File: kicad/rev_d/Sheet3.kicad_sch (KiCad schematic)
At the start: 118 parts, among them X10 ST-214C, X14 AAFP/AC97 headphones/tapein, X16 PLB1-4I, X17 PLB1-4I, X18 PLB1-4I, X20 PLB1-4I

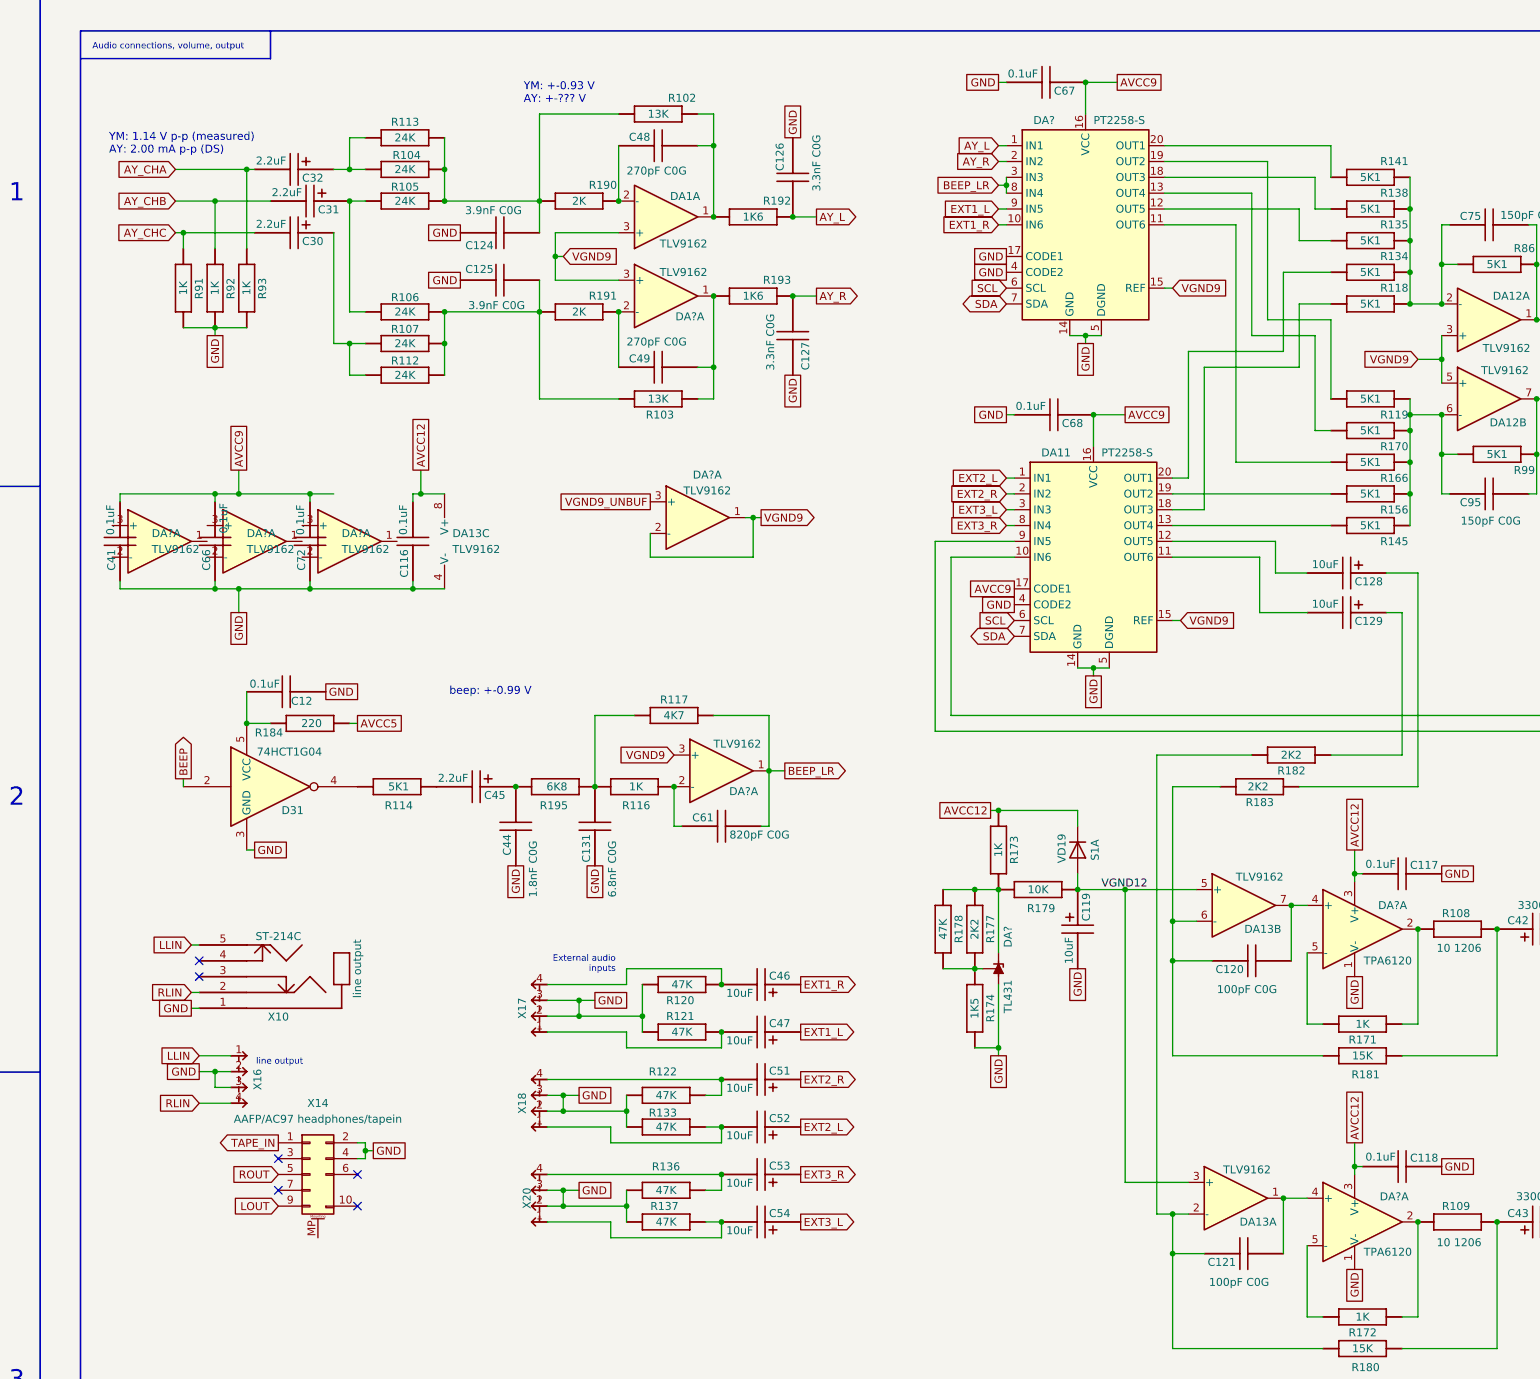
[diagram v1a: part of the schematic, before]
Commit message: pentevo: rev D: video output: remove 373/374 stuff (WIP); fix DA numbering issue
git-svn-id: svn://localhost/local-pentevo@1282 c6c76956-fad2-4150-a3a9-ea0a427205ba
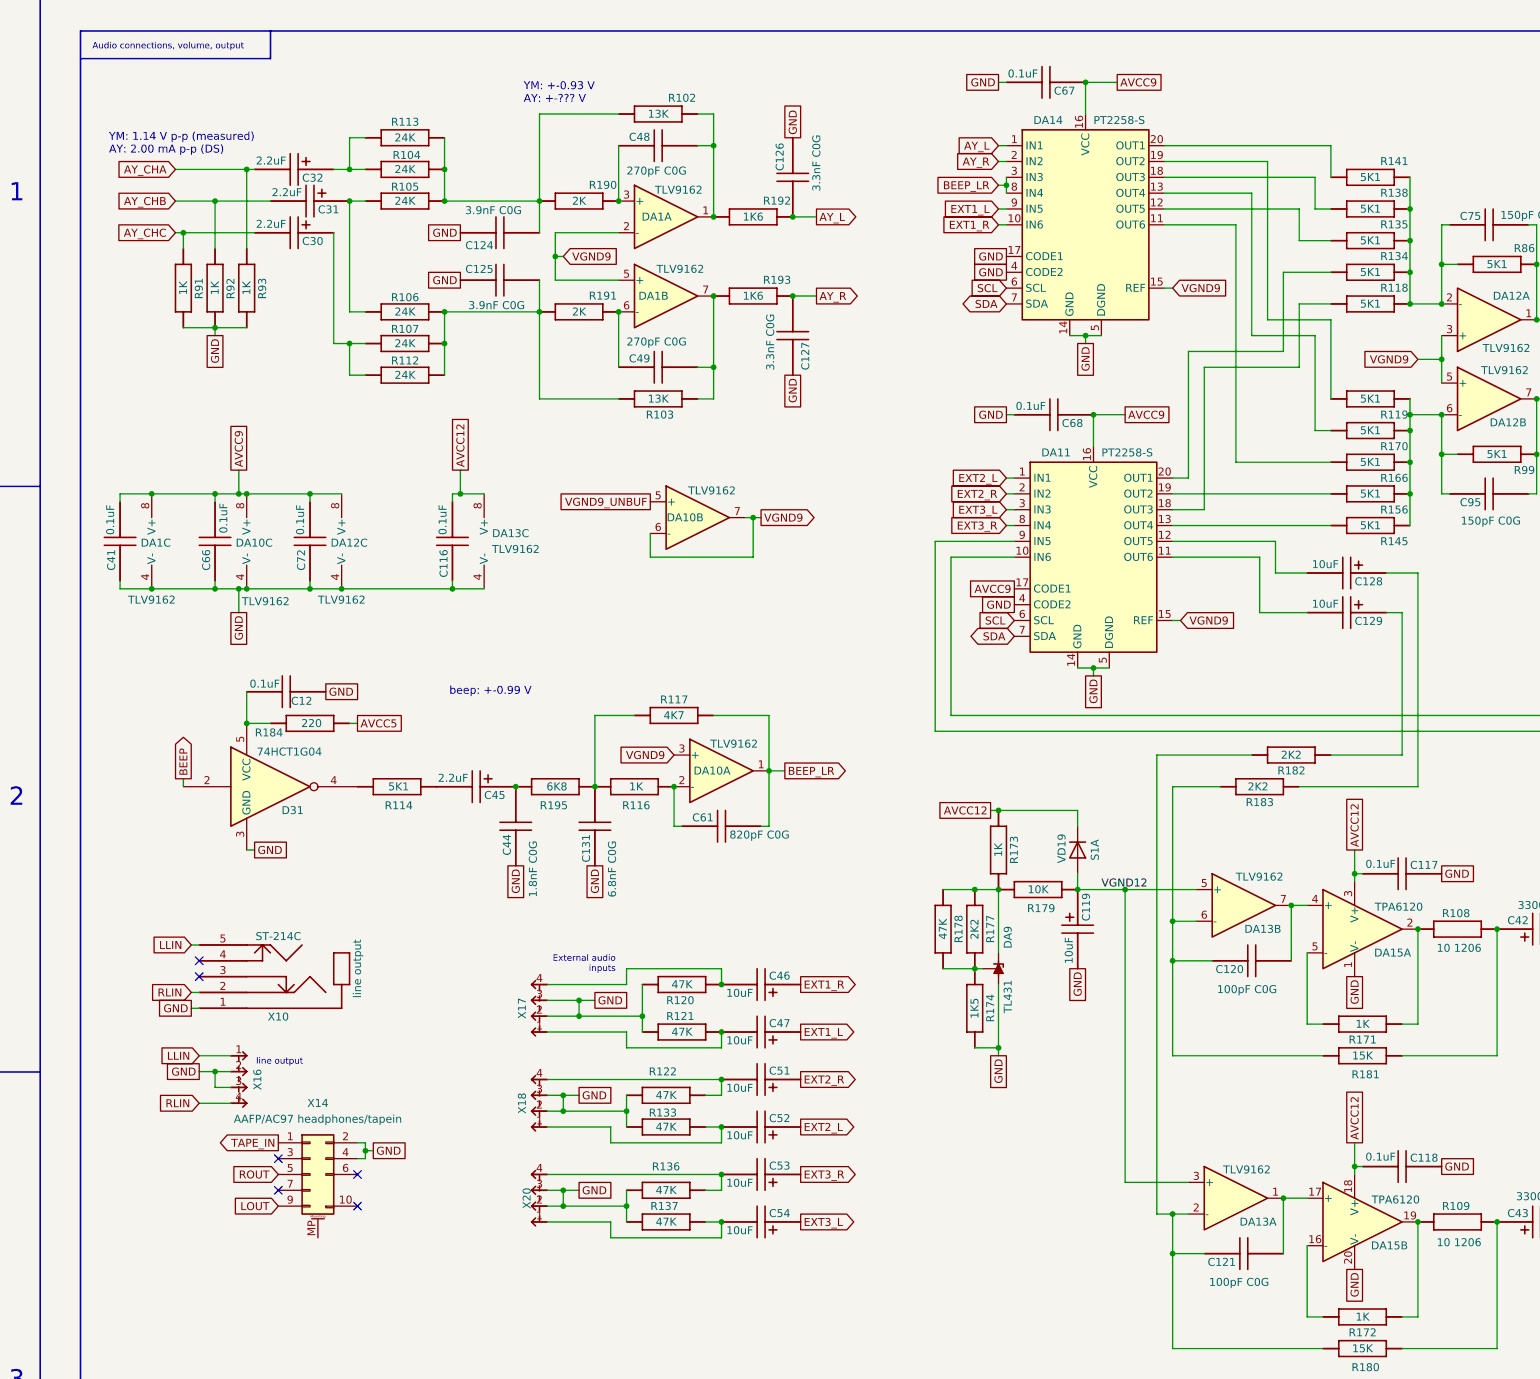
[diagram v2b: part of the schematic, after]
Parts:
- removed DA? (x6): TLV9162, symbol eva-altium-import:TLC072
- removed DA? (x2): TPA6120, symbol eva-altium-import:TPA6120
- added unit 2 of DA1
- added unit 3 of DA1
- added DA10: TLV9162, symbol eva-altium-import:TLC072
- added unit 3 of DA12
- added DA15: TPA6120, symbol tpa6120:TPA6120
- gave numbers to parts that had none: 2
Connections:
- net AVCC12: now also DA15.18 (V+), DA15.3 (V+)
- net AVCC9: now also DA1.8 (V+), DA10.8 (V+), DA12.8 (V+)
- net BEEP_LR: now also DA10.1
- net GND: now also DA1.4 (V-), DA10.4 (V-), DA12.4 (V-), DA15.1 (V-), DA15.20 (V-)
- net VGND9: now also DA1.2 (-), DA1.5 (+), DA10.3 (+), DA10.6 (-), DA10.7; no longer DA1.3 (+)
- net VGND9_UNBUF: now also DA10.5 (+)
- net at C61.1, R116.1 (i/o): now also DA10.2 (-)
- net at C121.2, DA13.1: now also DA15.17 (+)
- net at C120.2, DA13.7: now also DA15.4 (+)
- net at C48.1, R190.1 (i/o): now also DA1.3 (+); no longer DA1.2 (-)
- net at C49.2, R103.1 (i/o), R193.2 (i/o1): now also DA1.7
- net at C49.1, R191.1 (i/o): now also DA1.6 (-)
- net at R108.2 (i/o1), R171.1 (i/o): now also DA15.2
- net at R171.2 (i/o1): now also DA15.5 (-)
- net at R109.2 (i/o1), R172.1 (i/o): now also DA15.19
- net at R172.2 (i/o1): now also DA15.16 (-)
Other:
- moved on the sheet: C116, DA13C
